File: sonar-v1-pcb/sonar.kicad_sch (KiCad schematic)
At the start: 1 part

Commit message: added some adc shit
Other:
- added sheet power_supply (power_supply.kicad_sch)
- sheet eight_transducer_array ports: added -10V; removed 20V

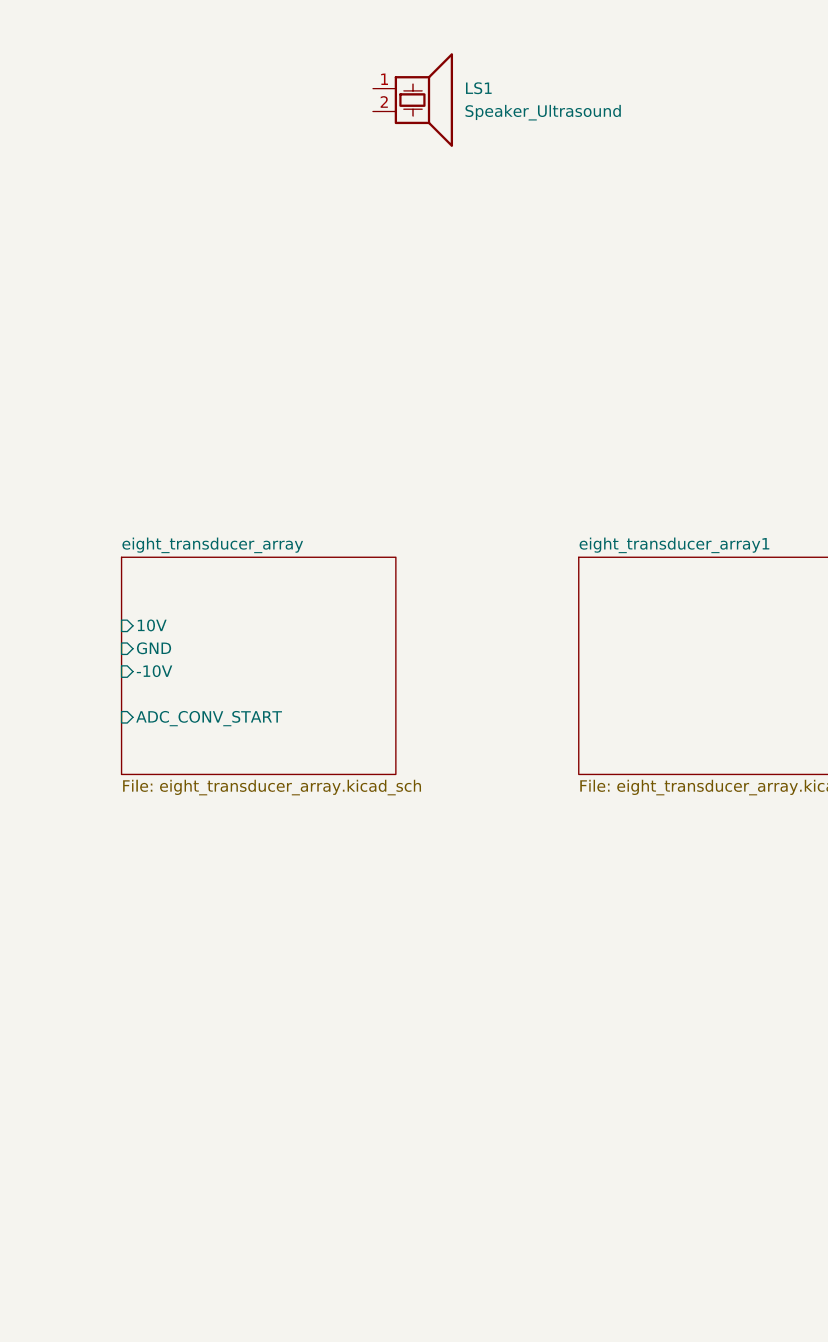
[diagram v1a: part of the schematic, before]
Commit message: fix bandpass
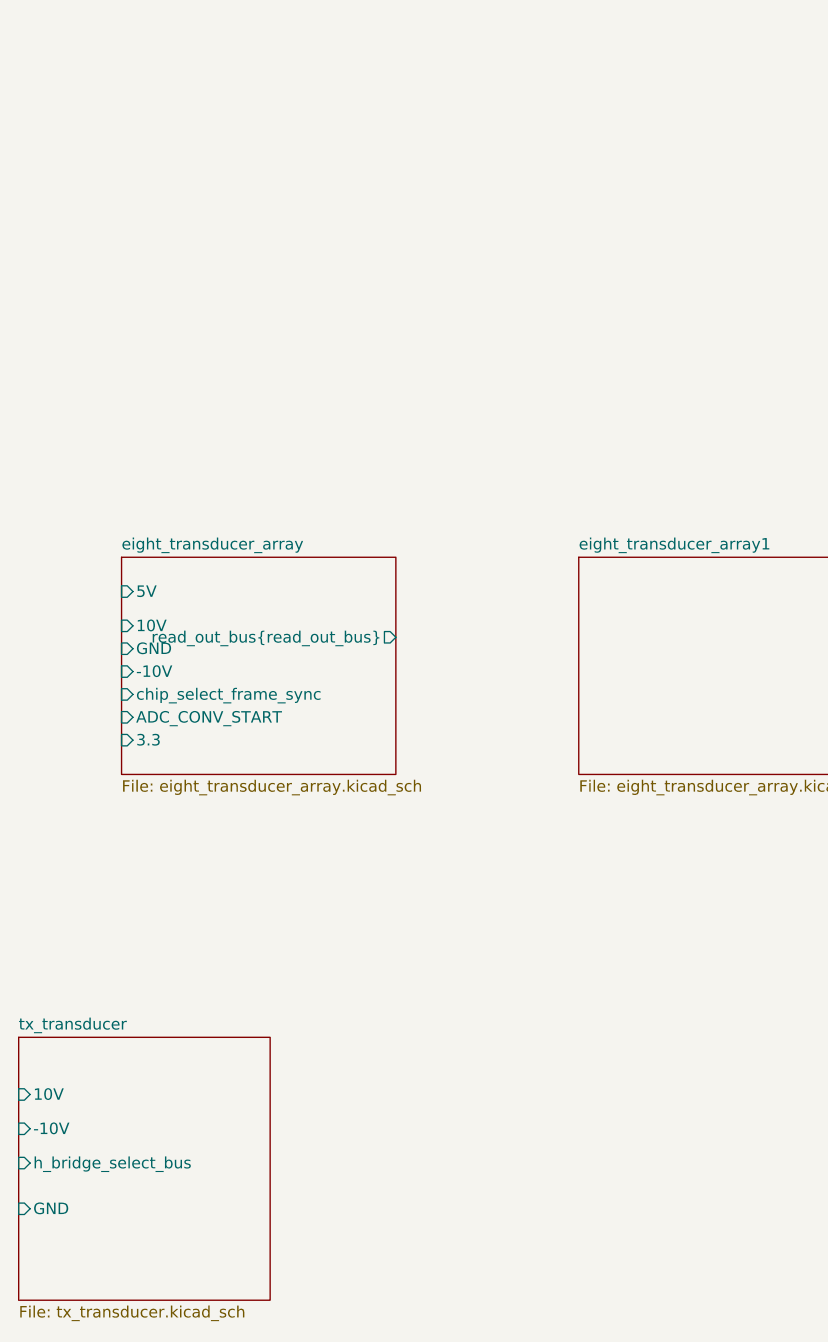
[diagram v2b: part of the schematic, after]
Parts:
- removed LS1: Speaker_Ultrasound, Sonar:MA40S4, symbol Device:Speaker_Ultrasound
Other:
- added sheet tx_transducer (tx_transducer.kicad_sch)
- sheet eight_transducer_array ports: added 3.3, 5V, chip_select_frame_sync, read_out_bus{read_out_bus}; removed none

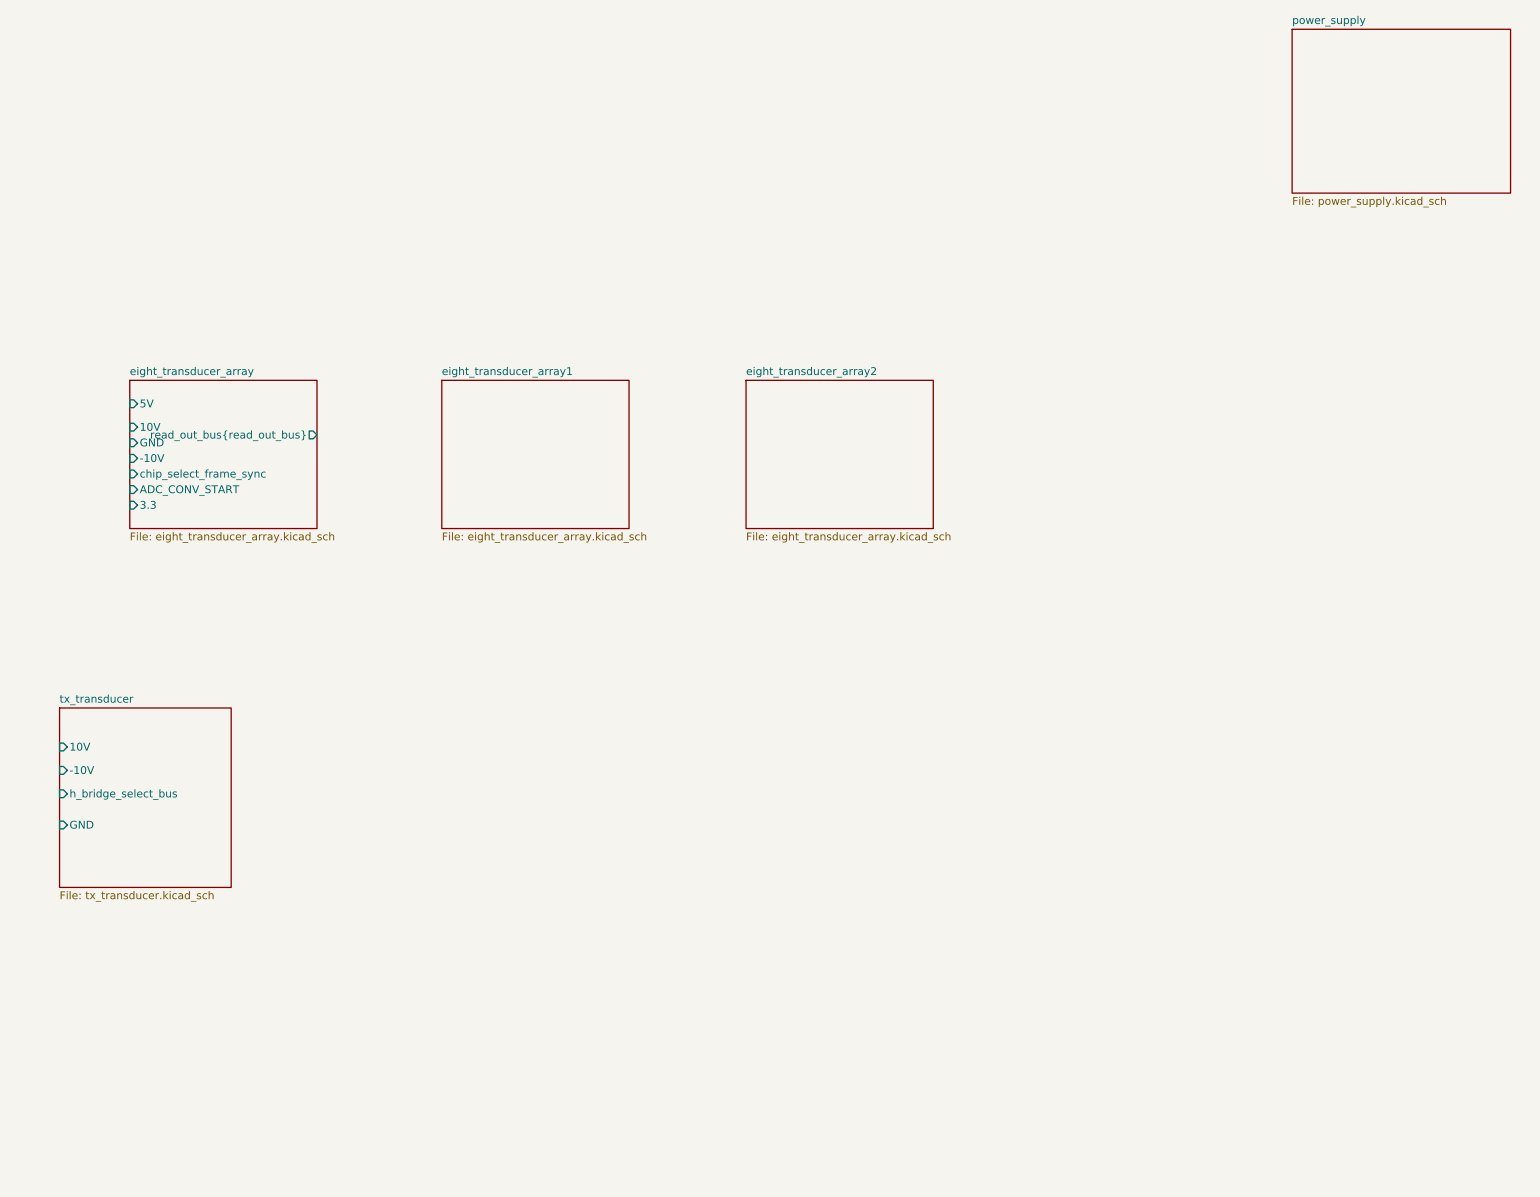
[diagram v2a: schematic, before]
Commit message: Add lowpas filter
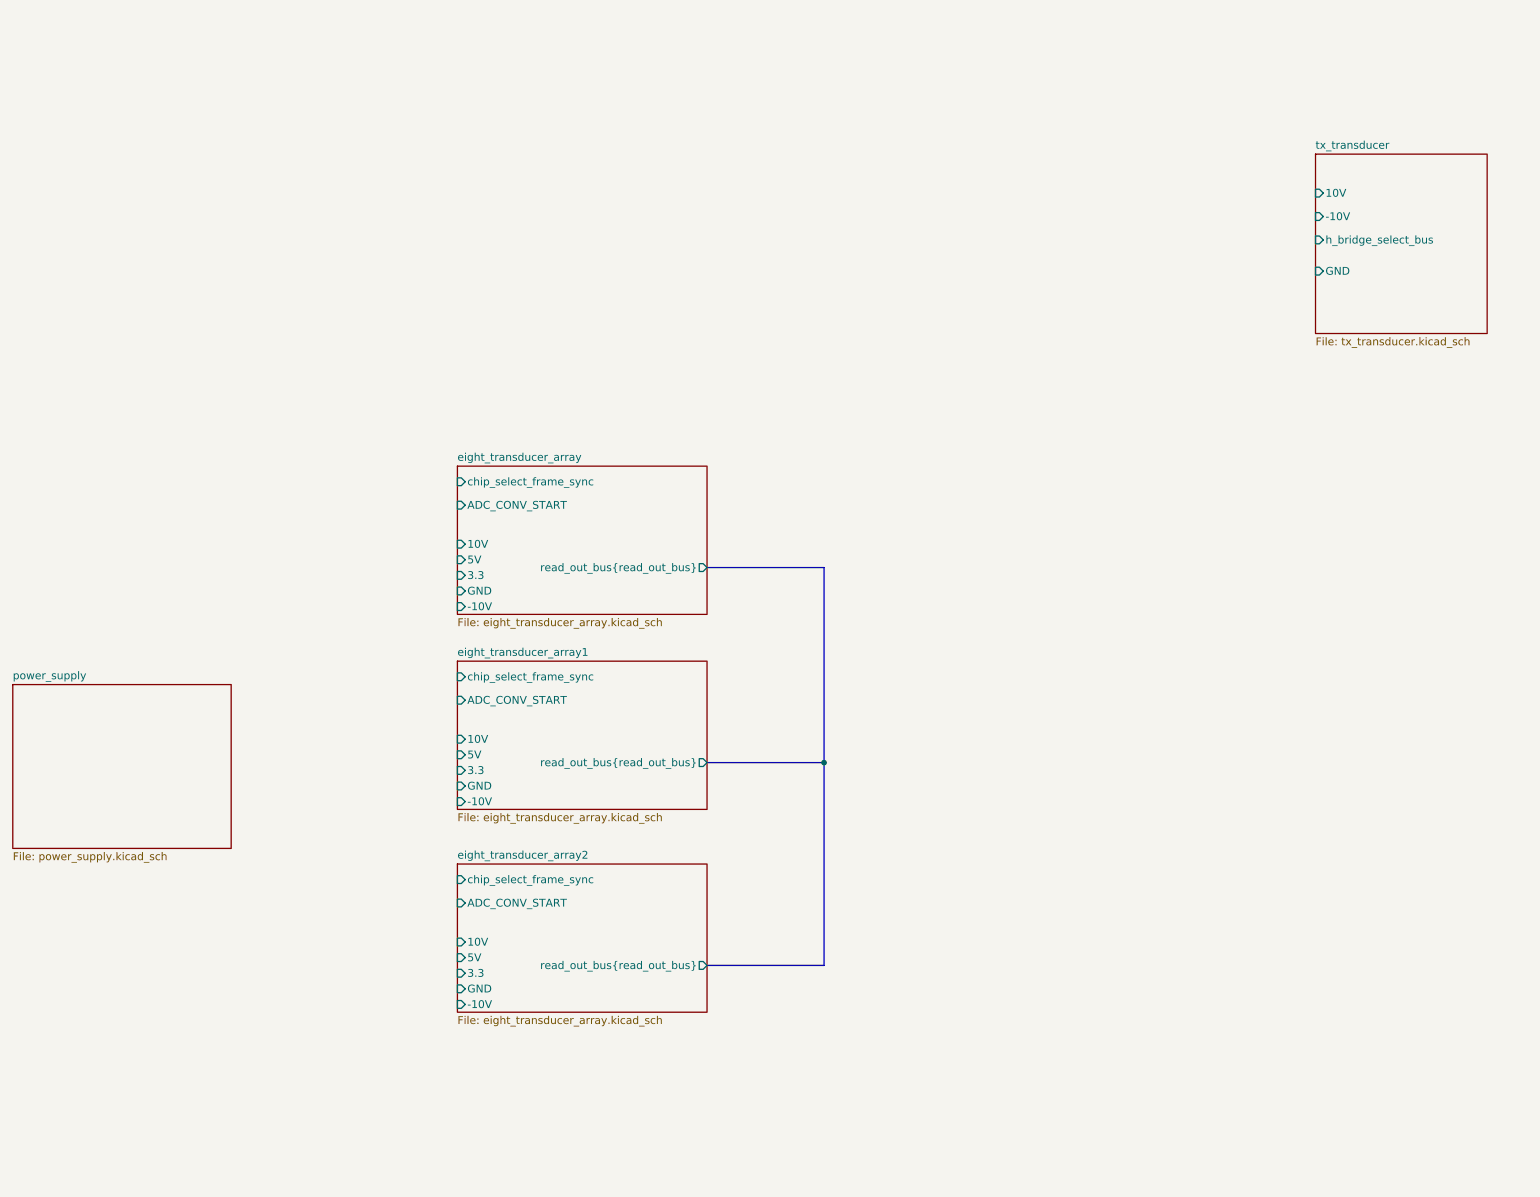
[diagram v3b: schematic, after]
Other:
- sheet eight_transducer_array1 ports: added -10V, 10V, 3.3, 5V, ADC_CONV_START, GND, chip_select_frame_sync, read_out_bus{read_out_bus}; removed none
- sheet eight_transducer_array2 ports: added -10V, 10V, 3.3, 5V, ADC_CONV_START, GND, chip_select_frame_sync, read_out_bus{read_out_bus}; removed none

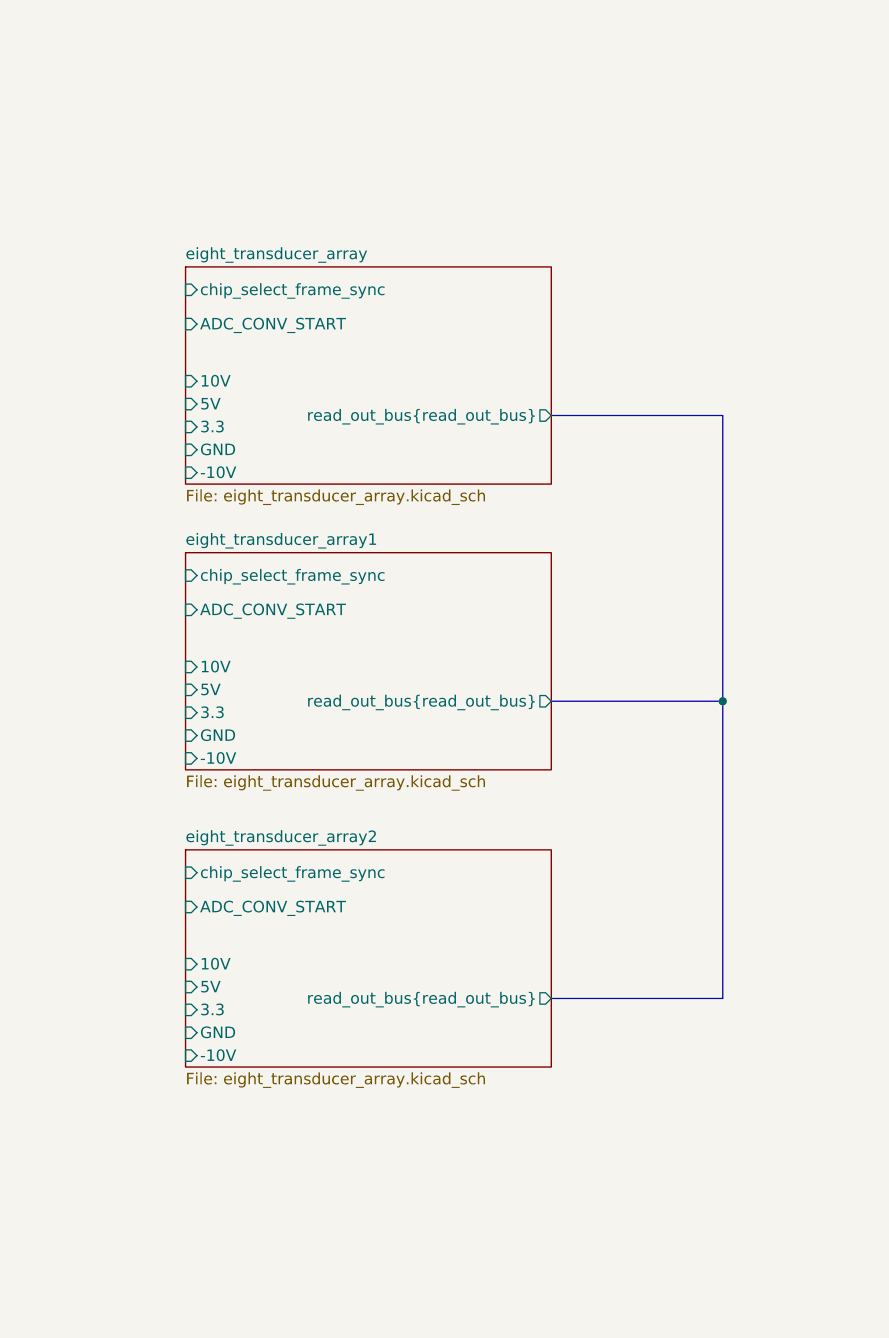
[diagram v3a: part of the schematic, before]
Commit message: finish ADC signals
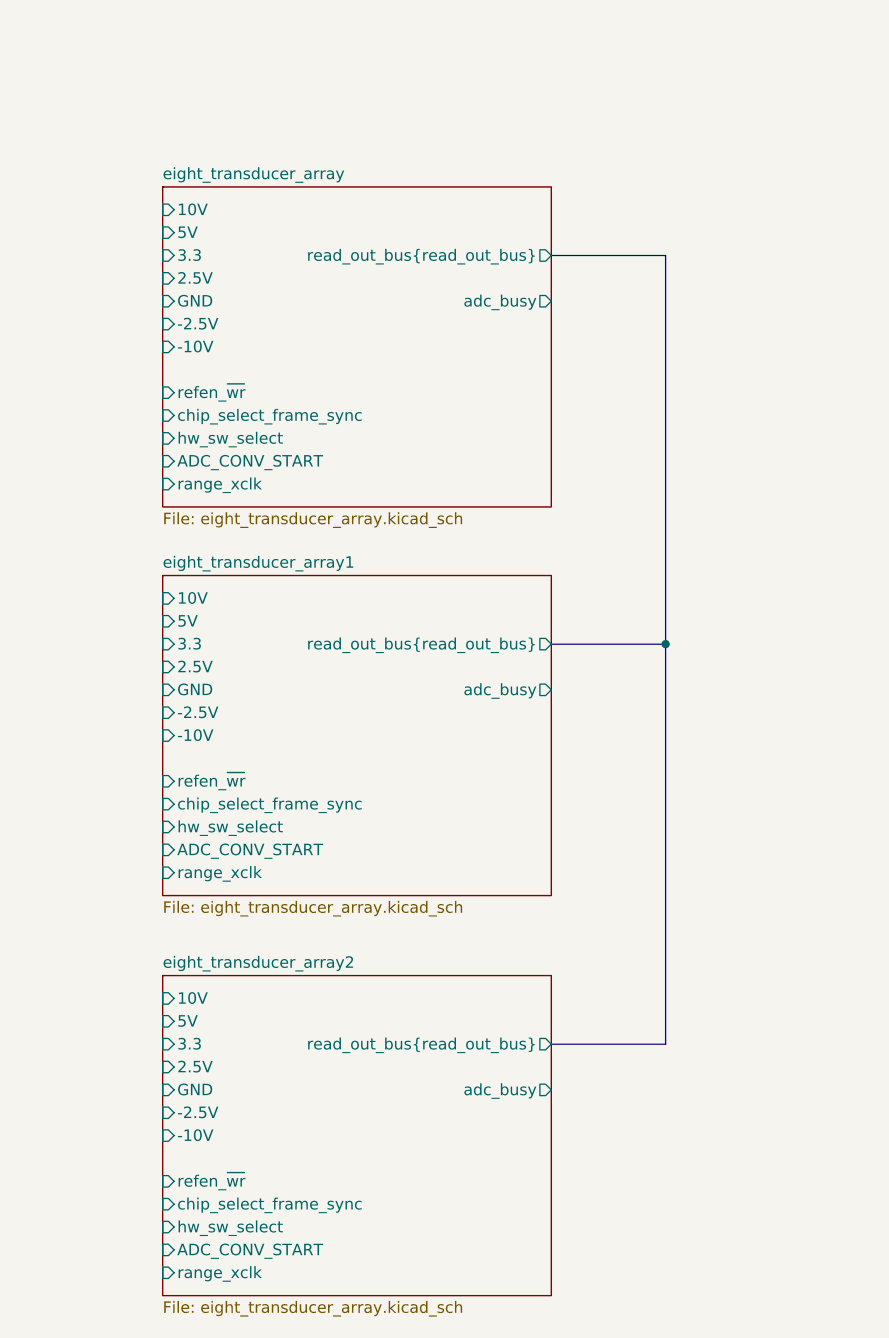
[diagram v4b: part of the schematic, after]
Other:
- sheet eight_transducer_array ports: added -2.5V, 2.5V, adc_busy, hw_sw_select, range_xclk, refen_~{wr}; removed none
- sheet eight_transducer_array1 ports: added -2.5V, 2.5V, adc_busy, hw_sw_select, range_xclk, refen_~{wr}; removed none
- sheet eight_transducer_array2 ports: added -2.5V, 2.5V, adc_busy, hw_sw_select, range_xclk, refen_~{wr}; removed none
